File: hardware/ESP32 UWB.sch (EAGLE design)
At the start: 52 parts, among them IC1 CP2104, J2 HEADER-12P-2.54, J3 USB-MICRO-5P, Q3 S8050, Q4 S8050, U2 ME6217C33M5G, U4 LD1117/3.3v, U5 DWM1000, U6 ESP32-C3-MINI-1-N4

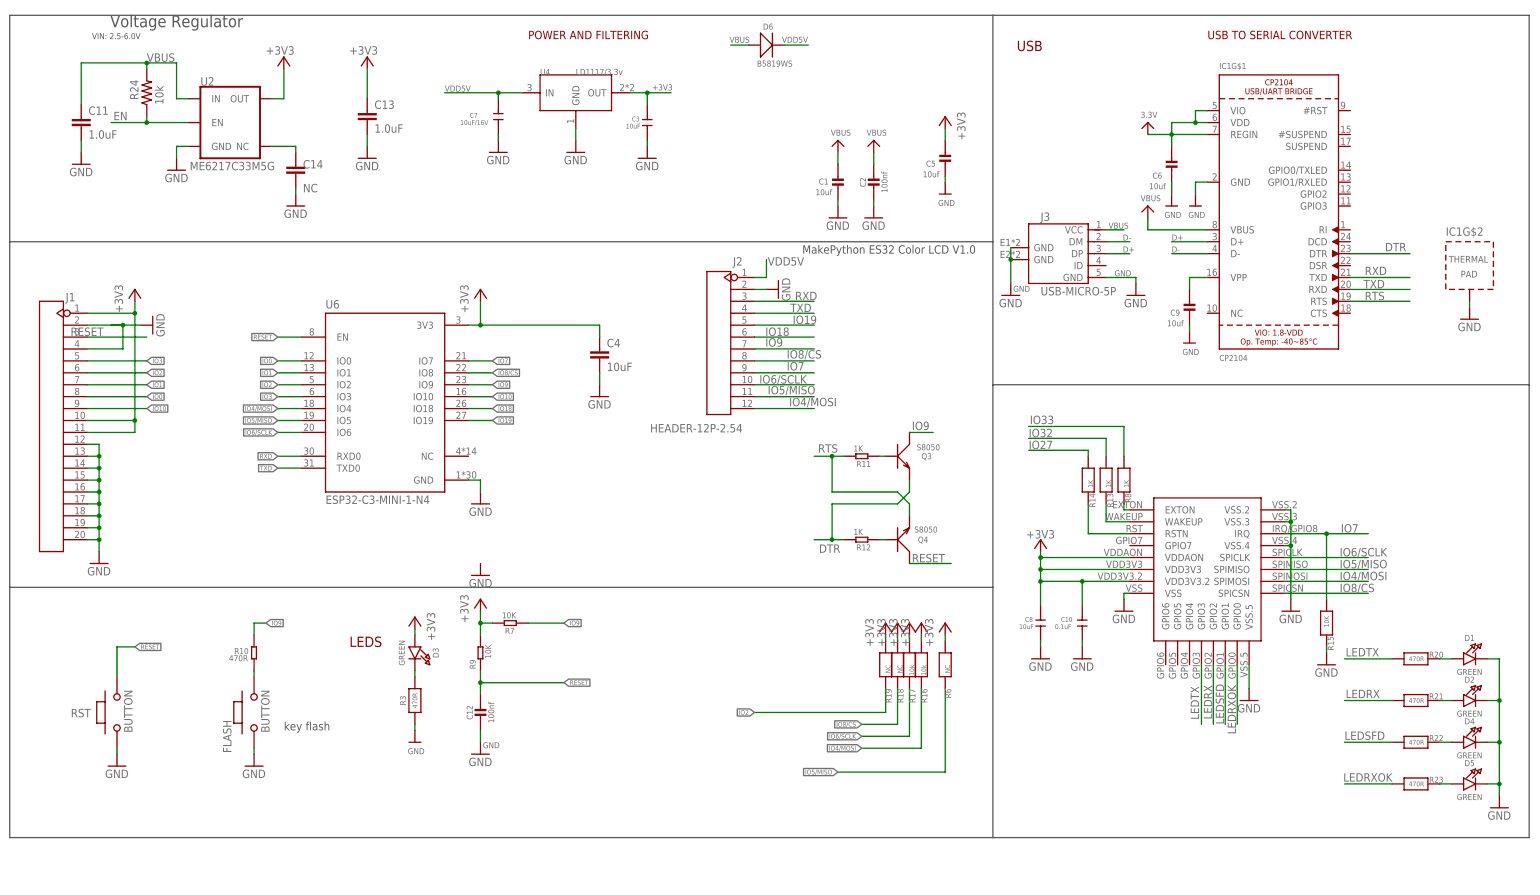
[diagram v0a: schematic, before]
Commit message: switched various parts to more newer or more available part, moved all to the front
Switched Parts:
*  USB-Serial Converter CP2104 -> CP2102N
*  3.3V LDO
*  Micro USB Connector

All parts are now on the front side which means expensive double sided assembly is no longer needed.
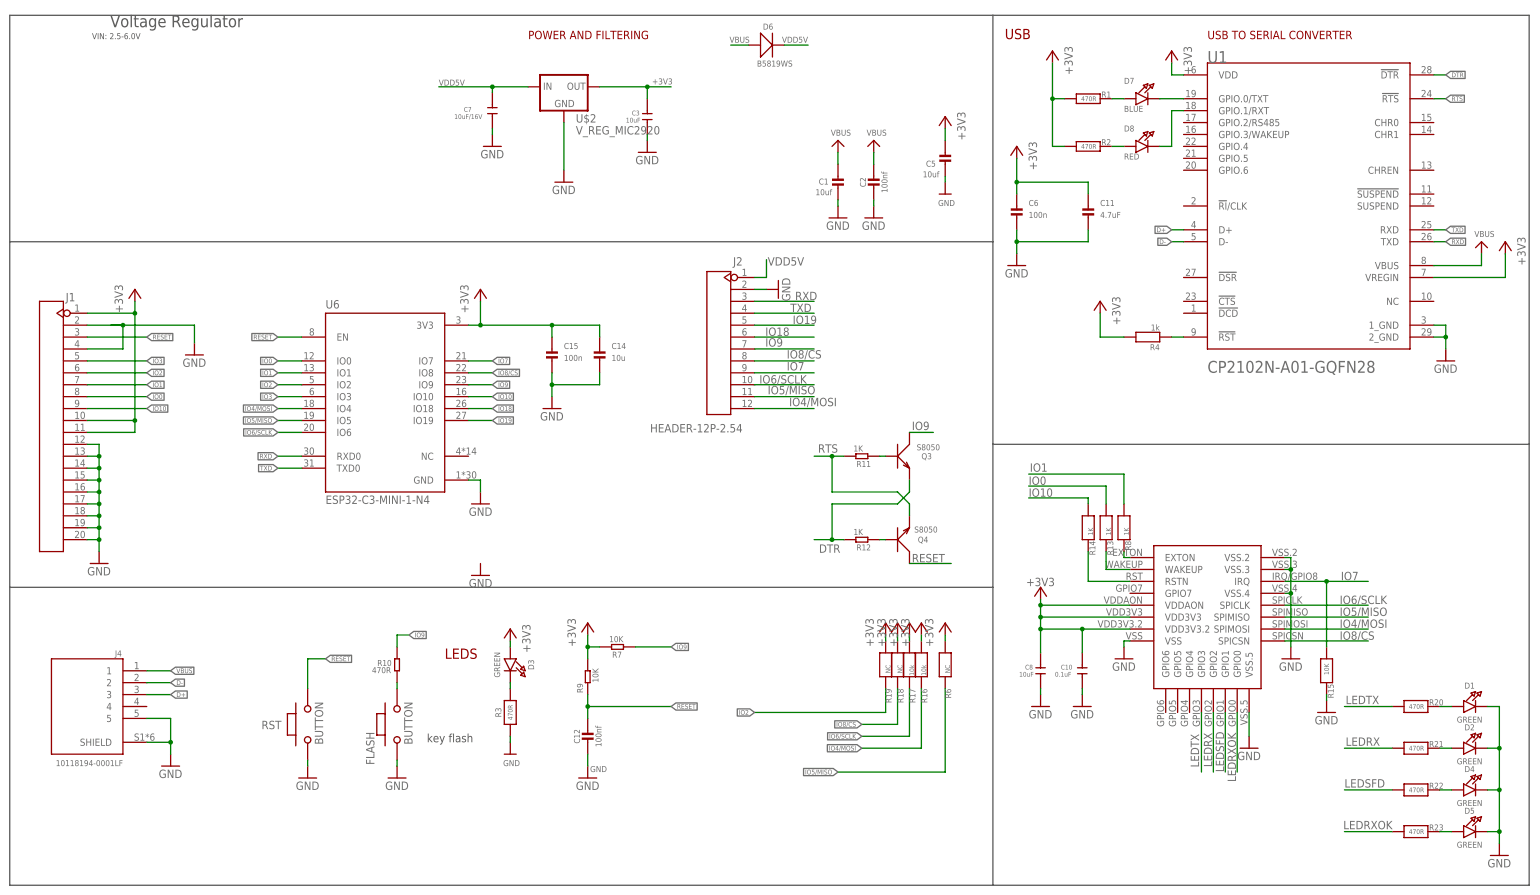
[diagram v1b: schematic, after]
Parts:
- removed C13: 1.0uF, SparkFun-Capacitors:1.0UF-0603-16V-10%
- removed C4: 10uF, rcl:C-EUC0603
- removed C9: 10uf, microbuilder:CAP_CERAMIC0603_NO
- removed IC1: CP2104, microbuilder:CP2104
- removed J3: USB-MICRO-5P, Connector:USB-MICRO-5P
- removed R24: 10k, SparkFun-Resistors:10KOHM-0603-1/10W-1%
- removed U2: ME6217C33M5G, SparkFun-IC-Power:V_REG_AP2112K-3.3V
- removed U4: LD1117/3.3v, IC:LD1117'SOT89'
- added C15: 100n, isystems:CAP_CERAMIC0603
- added D7: BLUE, isystems:LED0603_NOOUTLINE
- added D8: RED, isystems:LED0603_NOOUTLINE
- added J4: 10118194-0001LF, 10118194-0001LF:10118194-0001LF
- added R1, R2: 470R, isystems:RESISTOR_0603
- added R4: 1k, isystems:RESISTOR_0603
- added U$2: V_REG_MIC2920, SparkFun-PowerIC:V_REG_MIC2920
- added U1: SILICON_LABS_CP2102N-A01-GQFN28SILICON_LABS_CP2102N-A01-GQF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, Silicon Labs - CP2102N-A01-GQFN28:SILICON_LABS_CP2102N-A01-GQFN28SILICON_LABS_CP2102N-A01-GQFN28_0_3
- C11: value 1.0uF -> 4.7uF; device SparkFun-Capacitors:1.0UF-0603-16V-10% -> isystems:CAP_CERAMIC0603
- C14: value NC -> 10u; device SparkFun-Capacitors:1.0UF-0603-16V-10% -> isystems:CAP_CERAMIC0603; PROD_ID CAP-00868 -> (none); VALUE 1.0uF -> (none)
- C6: value 10uf -> 100n; device microbuilder:CAP_CERAMIC0603_NO -> isystems:CAP_CERAMIC0603
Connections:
- removed net EN: R24.1, U2.EN
- removed net IO27: R14.1
- removed net IO32: R13.1
- removed net IO33: R8.1
- new net N$4: D8.A, R2.2
- new net N$6: D8.C, U1.GPIO.1/RXT
- new net N$8: R4.1, U1.!RST!
- net +3V3: now also C11.P$1, C14.P$1, C15.P$1, C6.P$1, R1.1, R2.1, R4.2, U$2.OUT, U1.VDD, U1.VREGIN; no longer C13.1, C4.1, C6.1, IC1G$1.REGIN, IC1G$1.VDD, IC1G$1.VIO, U2.OUT, U4.OUT
- net D+: now also J4.3, U1.D+; no longer IC1G$1.D+, J3.DP
- net D-: now also J4.2, U1.D-; no longer IC1G$1.D-, J3.DM
- net DTR: now also U1.!DTR!; no longer IC1G$1.DTR
- net GND: now also C11.P$2, C14.P$2, C15.P$2, C6.P$2, J4.5, J4.SHIELD, U$2.GND, U1.1_GND, U1.2_GND; no longer C11.2, C13.2, C14.2, C4.2, C6.2, C9.2, IC1G$1.GND, IC1G$2.TP, J3.GND@1, J3.GND@2, J3.GND@3, U2.GND, U4.GND
- net IO0: now also R13.1
- net IO1: now also R8.1
- net IO10: now also R14.1
- net N$2: now also D7.A, R1.2; no longer C9.1, IC1G$1.VPP
- net N$3: now also D7.C, U1.GPIO.0/TXT; no longer C14.1, U2.NC
- net RTS: now also U1.!RTS!; no longer IC1G$1.RTS
- net RXD: now also U1.TXD; no longer IC1G$1.TXD
- net TXD: now also U1.RXD; no longer IC1G$1.RXD
- net VBUS: now also J4.1, U1.VBUS; no longer C11.1, IC1G$1.VBUS, J3.VCC, R24.2, U2.IN
- net VDD5V: now also U$2.IN; no longer U4.IN
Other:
- note removed: "MakePython ES32 Color LCD V1.0"
- moved on the sheet: C10, C11, C12, C14, C3, C6, C7, C8, D1, D2, D3, D4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

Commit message: switched resistor and capacitor footprints, placed labels
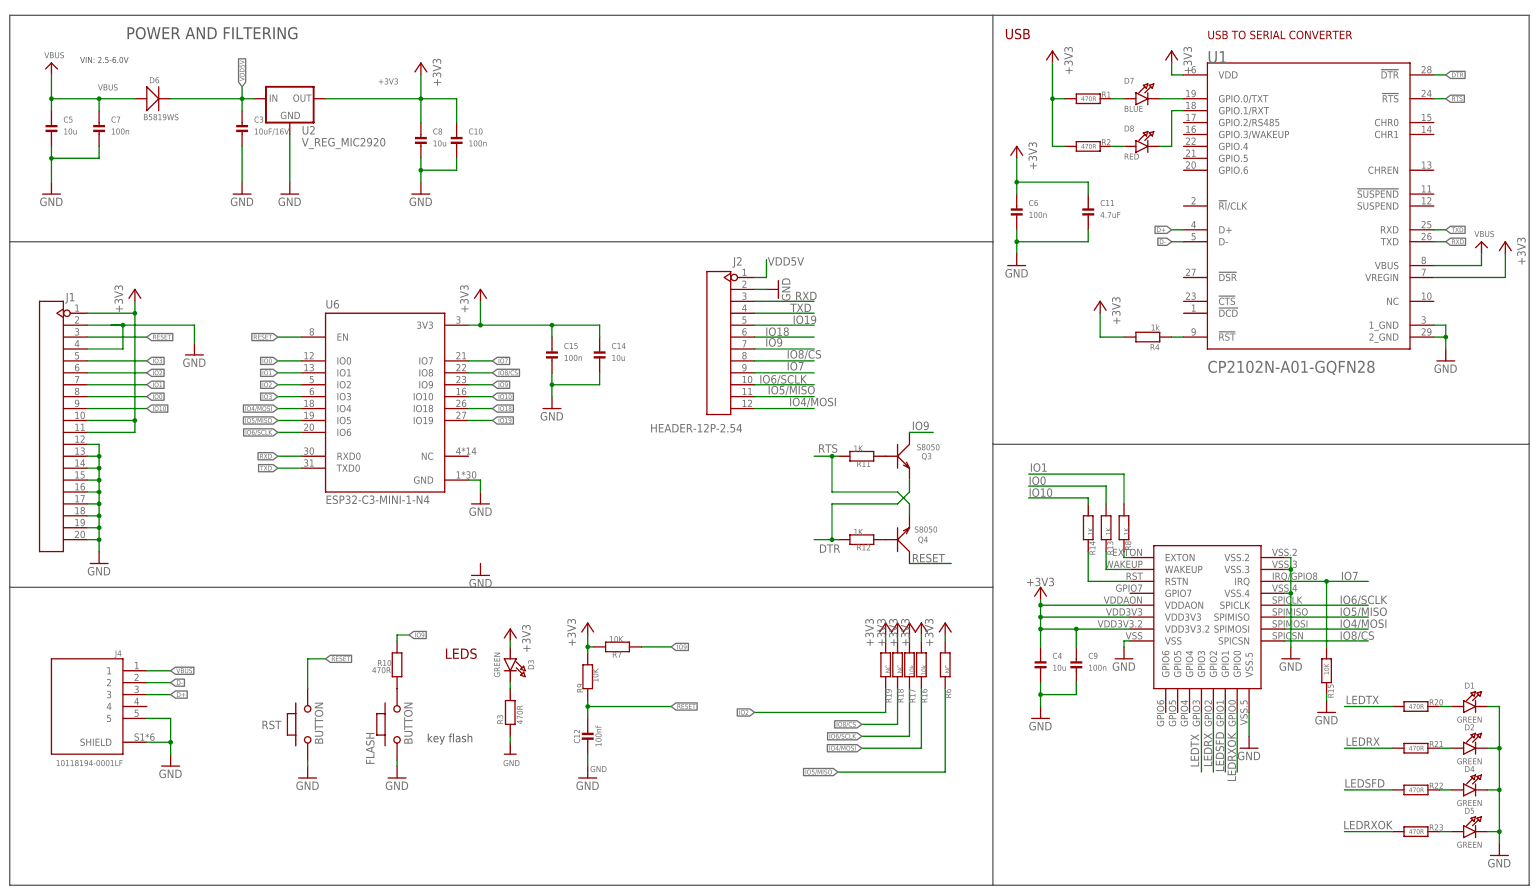
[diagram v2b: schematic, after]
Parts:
- removed C1: 10uf, microbuilder:CAP_CERAMIC0603_NO
- removed C2: 100nf, microbuilder:CAP_CERAMIC0603_NO
- removed U$2: V_REG_MIC2920, SparkFun-PowerIC:V_REG_MIC2920
- added C4: 10u, isystems:CAP_CERAMIC0603
- added C9: 100n, isystems:CAP_CERAMIC0603
- added U2: V_REG_MIC2920, SparkFun-PowerIC:V_REG_MIC2920
- C10: value 0.1uF -> 100n; device Discrete:C-0603 -> isystems:CAP_CERAMIC0603
- C3: value 10uF -> 10uF/16V; device Discrete:C-0603 -> isystems:CAP_CERAMIC0603
- C5: value 10uf -> 10u; device microbuilder:CAP_CERAMIC0603_NO -> isystems:CAP_CERAMIC0603
- C7: value 10uF/16V -> 100n; device Discrete:C-0603 -> isystems:CAP_CERAMIC0603
- C8: value 10uF -> 10u; device Discrete:C-0603 -> isystems:CAP_CERAMIC0603
- R1, R2, R4: device isystems:RESISTOR_0603 -> isystems:RESISTOR0603
- R10, R11, R12, R7, R9: device Discrete:R-0603 -> isystems:RESISTOR0603
- R13, R14, R15, R16, R17, R18, R19, R20, R21, R22, R23, R3, R6, R8: device microbuilder:RESISTOR_0603_NOOUT -> isystems:RESISTOR0603
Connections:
- net +3V3: now also C10.P$1, C4.P$1, C8.P$1, C9.P$1, U2.OUT; no longer C10.1, C3.1, C5.1, C8.1, U$2.OUT
- net GND: now also C10.P$2, C3.P$2, C4.P$2, C5.P$2, C7.P$2, C8.P$2, C9.P$2, U2.GND; no longer C1.2, C10.2, C2.2, C3.2, C5.2, C7.2, C8.2, U$2.GND
- net VBUS: now also C5.P$1, C7.P$1; no longer C1.1, C2.1
- net VDD5V: now also C3.P$1, U2.IN; no longer C7.1, U$2.IN
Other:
- note removed: "Voltage Regulator"
- moved on the sheet: C5, D6

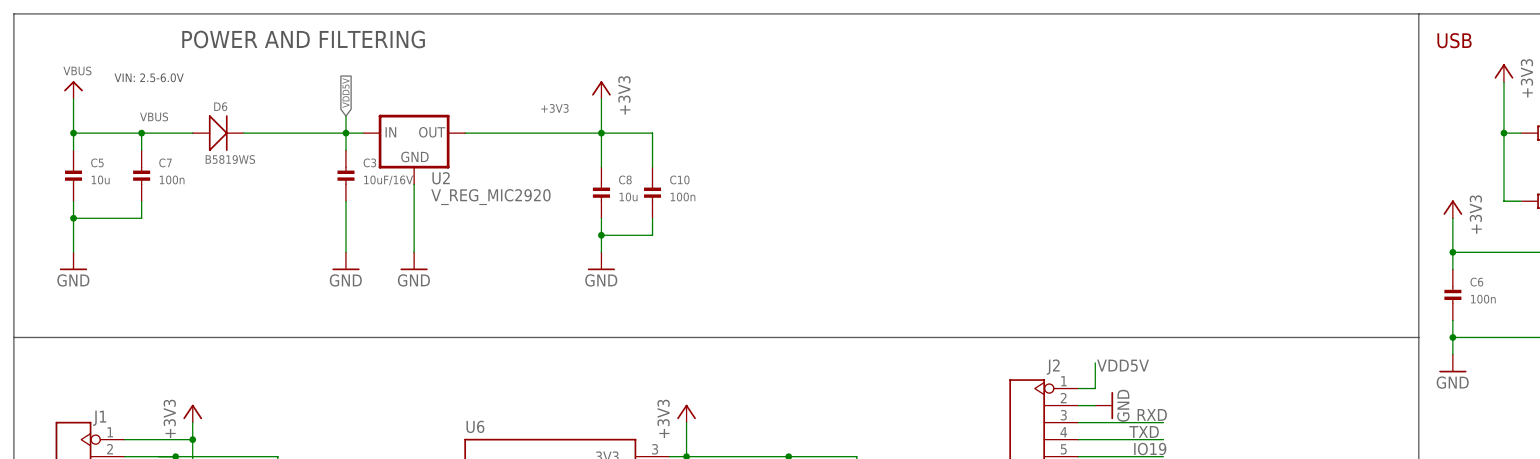
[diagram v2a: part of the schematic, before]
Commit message: Added WS2812b led for status display
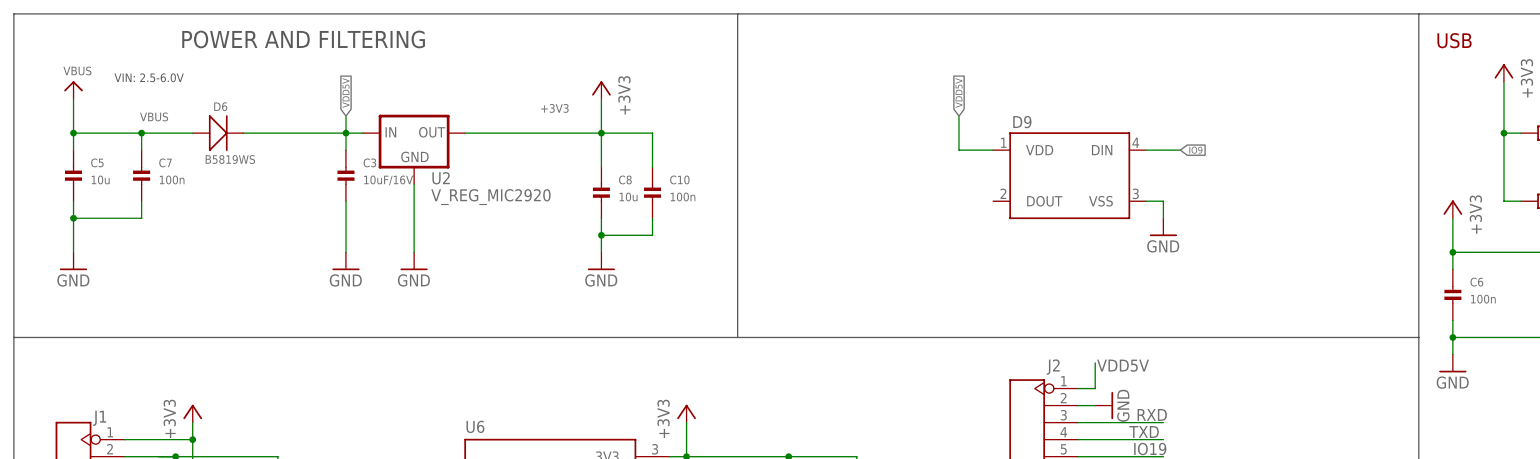
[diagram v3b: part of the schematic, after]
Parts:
- added D9: (no value), SparkFun-LED:WS2812B
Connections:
- net GND: now also D9.VSS
- net IO9: now also D9.DIN
- net VDD5V: now also D9.VDD
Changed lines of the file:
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@@
 <part name="C5" library="isystems" deviceset="CAP_CERAMIC" device="0603" value="10u"/>
 <part name="C7" library="isystems" deviceset="CAP_CERAMIC" device="0603" value="100n"/>
+<part name="D9" library="SparkFun-LED" deviceset="WS2812B" device=""/>
+<part name="GND4" library="supply1" deviceset="GND" device=""/>
 </parts>
 <sheets>
@@
 <wire x1="434.34" y1="83.82" x2="434.34" y2="175.26" width="0.1524" layer="97"/>
 <wire x1="434.34" y1="175.26" x2="320.04" y2="175.26" width="0.1524" layer="97"/>
-<wire x1="320.04" y1="175.26" x2="110.49" y2="175.26" width="0.1524" layer="97"/>
+<wire x1="320.04" y1="175.26" x2="218.44" y2="175.26" width="0.1524" layer="97"/>
+<wire x1="218.44" y1="175.26" x2="110.49" y2="175.26" width="0.1524" layer="97"/>
 <wire x1="110.49" y1="175.26" x2="110.49" y2="127" width="0.1524" layer="97"/>
 <wire x1="110.49" y1="127" x2="110.49" y2="53.34" width="0.1524" layer="97"/>
@@
 <wire x1="320.04" y1="83.82" x2="320.04" y2="53.34" width="0.1524" layer="97"/>
 <wire x1="320.04" y1="83.82" x2="434.34" y2="83.82" width="0.1524" layer="97"/>
-<wire x1="110.49" y1="127" x2="320.04" y2="127" width="0.1524" layer="97"/>
+<wire x1="110.49" y1="127" x2="218.44" y2="127" width="0.1524" layer="97"/>
 <text x="199.39" y="20.32" size="1.778" layer="97">key flash</text>
 <text x="153.67" y="171.45" size="2.54" layer="97" font="vector" align="center">POWER AND FILTERING</text>
 <text x="125.476" y="165.1" size="1.27" layer="97" font="vector">VIN: 2.5-6.0V</text>
+<wire x1="218.44" y1="127" x2="320.04" y2="127" width="0.1524" layer="97"/>
+<wire x1="218.44" y1="175.26" x2="218.44" y2="127" width="0.1524" layer="97"/>
 </plain>
 <instances>
@@
 <instance part="C5" gate="G$1" x="119.38" y="149.86"/>
 <instance part="C7" gate="G$1" x="129.54" y="149.86"/>
+<instance part="D9" gate="G$1" x="261.62" y="149.86"/>
+<instance part="GND4" gate="1" x="281.94" y="142.24"/>
 </instances>
 <busses>
@@
 <junction x="119.38" y="144.78"/>
 </segment>
+<segment>
+<pinref part="GND4" gate="1" pin="GND"/>
+<pinref part="D9" gate="G$1" pin="VSS"/>
+<wire x1="281.94" y1="144.78" x2="281.94" y2="147.32" width="0.1524" layer="91"/>
+<wire x1="281.94" y1="147.32" x2="279.4" y2="147.32" width="0.1524" layer="91"/>
+</segment>
 </net>
 <net name="+3V3" class="0">
@@
 <wire x1="269.24" y1="119.38" x2="271.78" y2="119.38" width="0.1524" layer="91"/>
 </segment>
+<segment>
+<pinref part="D9" gate="G$1" pin="VDD"/>
+<wire x1="256.54" y1="154.94" x2="251.46" y2="154.94" width="0.1524" layer="91"/>
+<wire x1="251.46" y1="154.94" x2="251.46" y2="160.02" width="0.1524" layer="91"/>
+<label x="251.46" y="160.02" size="1.016" layer="95" rot="R90" xref="yes"/>
+</segment>
 </net>
 <net name="N$15" class="0">
@@
 <label x="271.526" y="104.648" size="1.778" layer="95"/>
 </segment>
-</net>
+<segment>
+<pinref part="D9" gate="G$1" pin="DIN"/>
+<wire x1="279.4" y1="154.94" x2="284.48" y2="154.94" width="0.1524" layer="91"/>
+<label x="284.48" y="154.94" size="1.016" layer="95" xref="yes"/>
+</segment>
+</net>
